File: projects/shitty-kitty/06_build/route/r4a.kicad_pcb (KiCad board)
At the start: 4 copper layers, 130 x 75 mm, 82 parts, among them J1 DC-005C-20A 12V, J2 TYPE-C-31-M-12, J3 ELECTRODES INNER, J4 ELECTRODES OUTER, J5 MOTOR NEMA17, J6 ENDSTOP TERM, J8 HOST 1x6, Q1 AOD4185 revpol, SW1 TS-1187A BOOT, SW2 TS-1187A RESET, U1 ESP32-S3-WROOM-1-N8R2, U2 TMC2209-LA-T, U3 MPR121QR2 0x5A, U4 MPR121QR2 0x5B, U5 MPR121QR2 0x5C, U6 MPR121QR2 0x5D, U7 LIS2DH12TR, U8 AP63205WU-7, U9 AMS1117-3.3

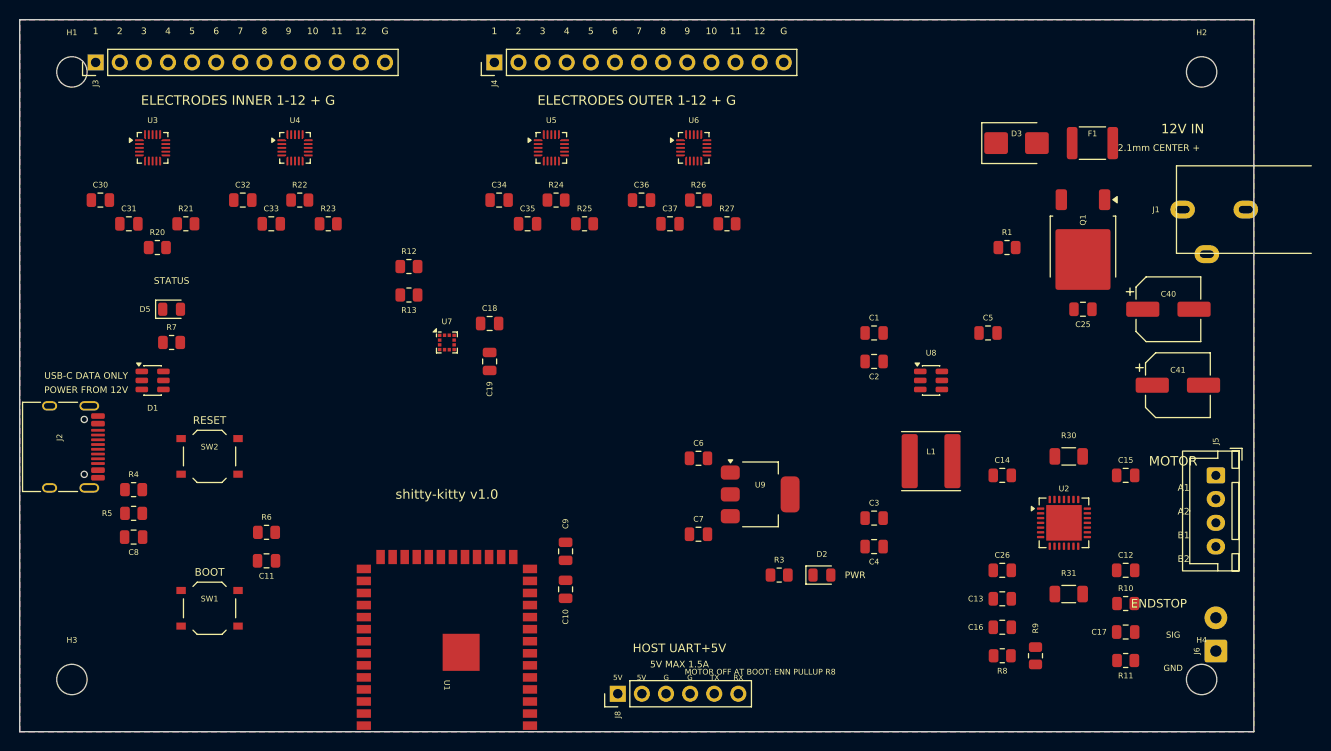
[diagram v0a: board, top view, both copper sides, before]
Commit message: shitty-kitty: routing campaign fixes — fab-floor rules (JLC 4L 3.5mil), grid-step 0.05 waves, escape-order reorder, placement round (J3 vs screw keepout, J1 edge-flush, U1 pad-edge window, J6/H4, silk de-collisions); COST_ESTIMATE + CHECKLIST drafts
Co-Authored-By: Claude Fable 5 <noreply@anthropic.com>
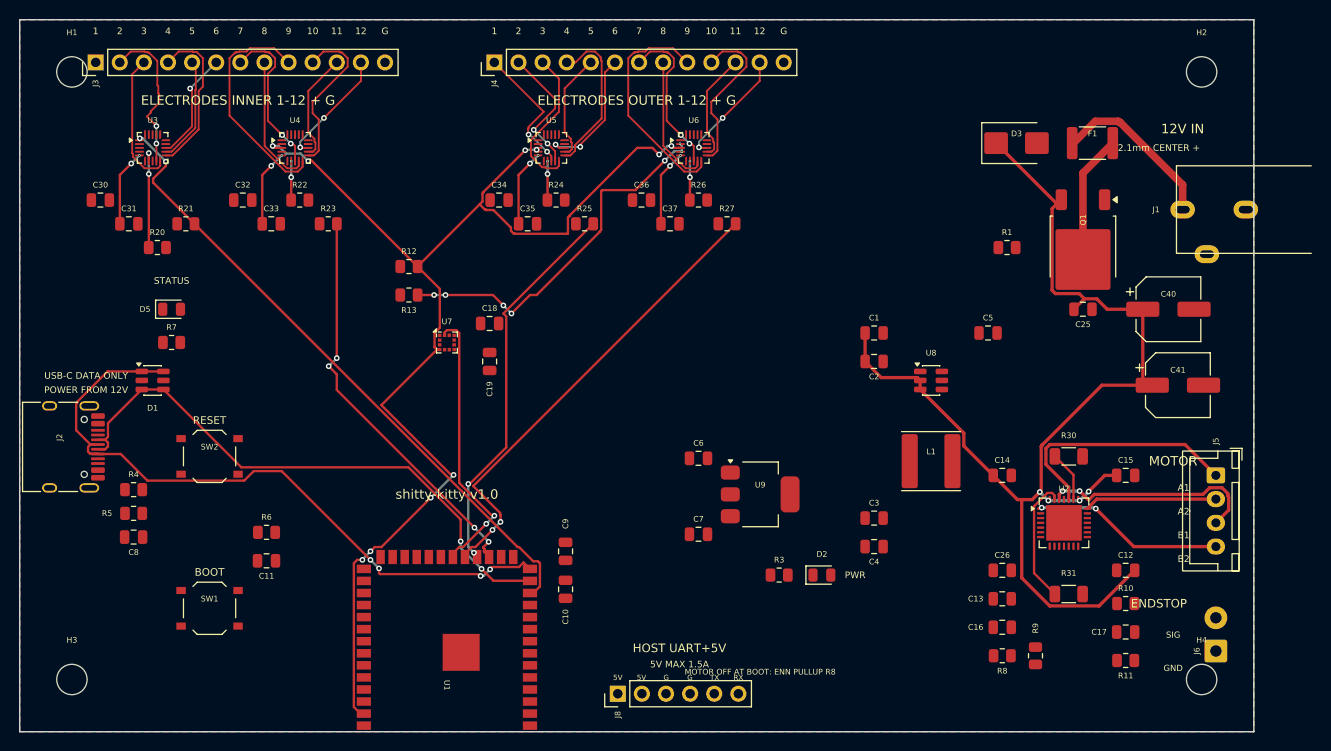
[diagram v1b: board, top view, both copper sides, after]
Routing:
- net SDA: track 0.00 -> 128.7 mm, vias 0 -> 10
- net VIN_12V: track 0.00 -> 120.3 mm, vias 0 -> 4
- net USB_DP: track 0.00 -> 71.2 mm, vias 0 -> 4
- net MPR_IRQ1: track 0.00 -> 67.9 mm, vias 0 -> 2
- net USB_DM: track 0.00 -> 60.6 mm, vias 0 -> 2
- net MPR_IRQ4: track 0.00 -> 49.5 mm, vias 0 -> 2
- net MPR_IRQ2: track 0.00 -> 43.0 mm, vias 0 -> 4
- net MPR_IRQ3: track 0.00 -> 41.3 mm, vias 0 -> 2
- net SCL: track 0.00 -> 39.2 mm, vias 0 -> 7
- net ACC_INT: track 0.00 -> 29.4 mm, vias 0 -> 2
- net MOT_A1: track 0.00 -> 25.8 mm
- net OUTER9: track 0.00 -> 24.3 mm
- net INNER9: track 0.00 -> 24.3 mm
- net MOT_B1: track 0.00 -> 23.3 mm, vias 0 -> 2
- net MOT_B2: track 0.00 -> 19.9 mm, vias 0 -> 2
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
